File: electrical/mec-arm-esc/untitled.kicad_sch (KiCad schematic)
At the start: 1 part, among them U2 STM32G474RET3

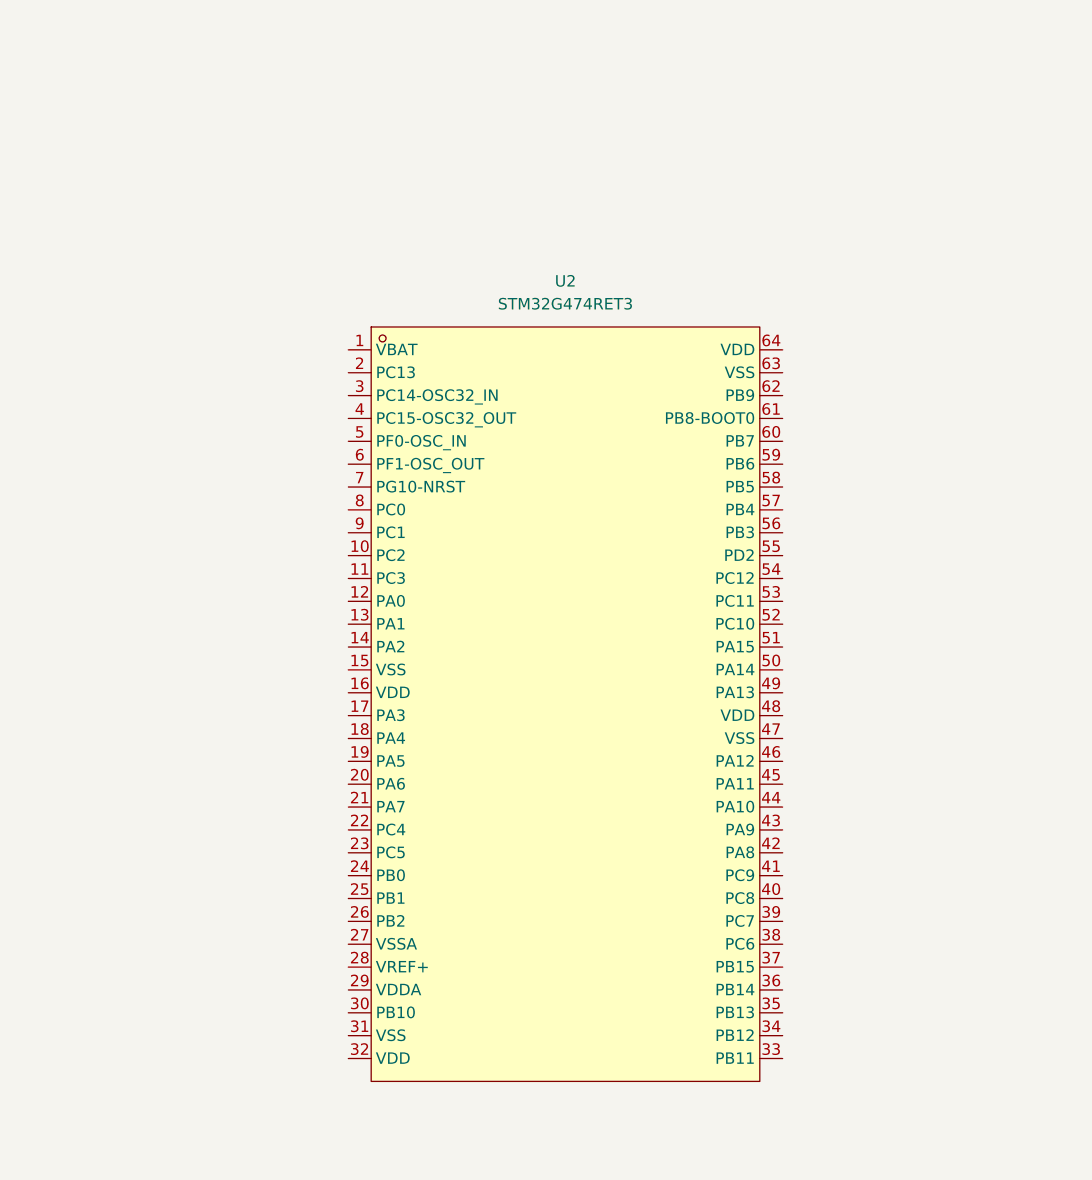
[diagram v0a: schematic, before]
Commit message: added MCU power and ground + altered symbol
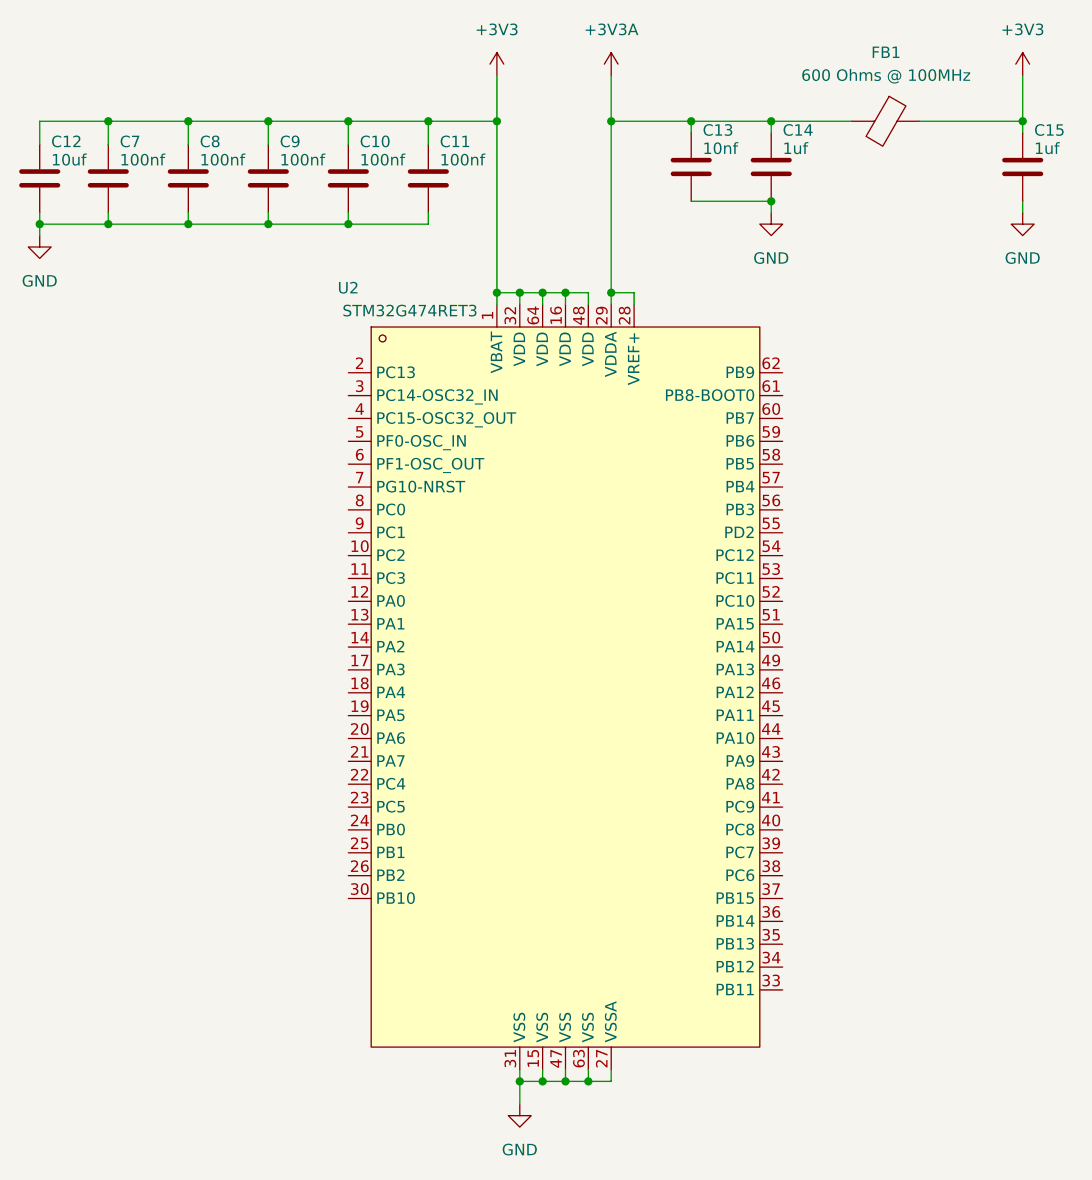
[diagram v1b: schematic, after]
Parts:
- added C10, C11, C7, C8, C9: 100nf, symbol Device:C
- added C12: 10uf, symbol Device:C
- added C13: 10nf, symbol Device:C
- added C14, C15: 1uf, symbol Device:C
- added FB1: 600 Ohms @ 100MHz, symbol Device:FerriteBead
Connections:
- net +3V3: now reaches U2.1 (VBAT)
- net +3V3: now also U2.16 (VDD), U2.32 (VDD), U2.48 (VDD), U2.64 (VDD), C10.1, C11.1, C12.1, C15.1, C7.1, C8.1, C9.1, FB1.1
- net GND: now reaches U2.15 (VSS)
- net GND: now also U2.27 (VSSA), U2.31 (VSS), U2.47 (VSS), U2.63 (VSS), C10.2, C11.2, C12.2, C13.2, C14.2, C15.2, C7.2, C8.2, C9.2
- net +3V3A: now reaches U2.28 (VREF+)
- net +3V3A: now also U2.29 (VDDA), C13.1, C14.1, FB1.2
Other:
- moved on the sheet: U2
